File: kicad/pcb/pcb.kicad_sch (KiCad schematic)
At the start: 0 parts

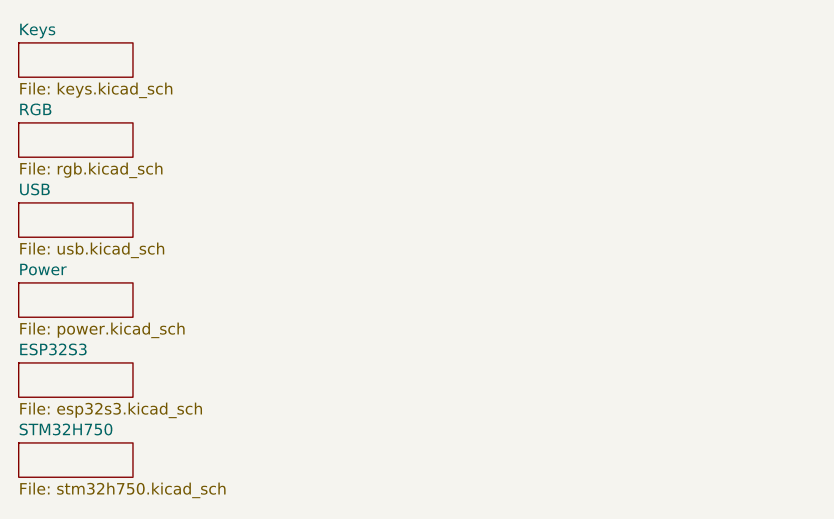
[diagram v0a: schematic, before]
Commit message: USB (almost) done + some STM progress
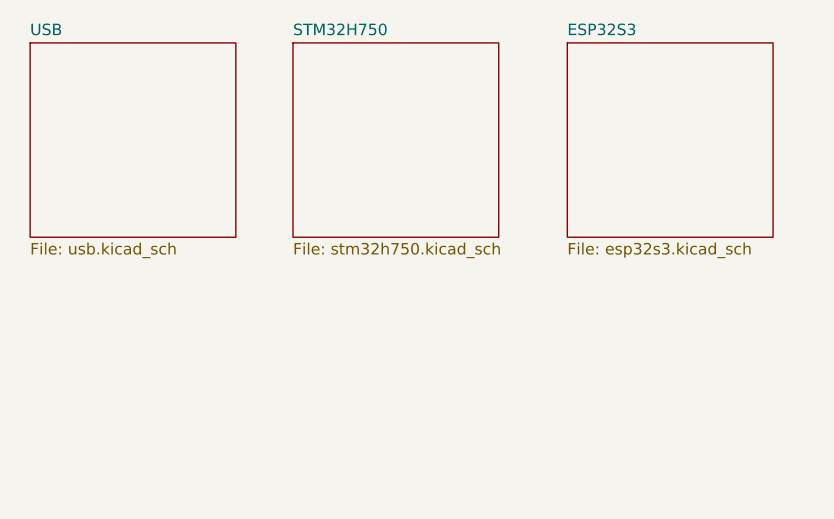
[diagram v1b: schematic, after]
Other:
- removed sheet Keys
- removed sheet Power
- removed sheet RGB
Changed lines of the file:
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@@
 (kicad_sch (version 20230121) (generator eeschema)
   (paper "A5")
-  (sheet (at 13.97 59.69) (size 12.7 3.81) (fields_autoplaced)
+  (sheet (at 44.45 15.24) (size 22.86 21.59) (fields_autoplaced)
     (stroke (width 0.1524) (type solid))
     (fill (color 0 0 0 0.0000))
-    (property "Sheetname" "STM32H750" (at 13.97 58.9784 0)
+    (property "Sheetname" "STM32H750" (at 44.45 14.5284 0)
       (effects (font (size 1.27 1.27)) (justify left bottom))
     )
-    (property "Sheetfile" "stm32h750.kicad_sch" (at 13.97 64.0846 0)
+    (property "Sheetfile" "stm32h750.kicad_sch" (at 44.45 37.4146 0)
       (effects (font (size 1.27 1.27)) (justify left top))
     )
     (instances
       (project "pcb"
-        (path "/3c00b562-f31c-4144-9978-9a1bbba7ab3a" (page "8"))
+        (path "/3c00b562-f31c-4144-9978-9a1bbba7ab3a" (page "2"))
       )
     )
   )
-  (sheet (at 13.97 24.13) (size 12.7 3.81) (fields_autoplaced)
+  (sheet (at 74.93 15.24) (size 22.86 21.59) (fields_autoplaced)
     (stroke (width 0.1524) (type solid))
     (fill (color 0 0 0 0.0000))
-    (property "Sheetname" "RGB" (at 13.97 23.4184 0)
+    (property "Sheetname" "ESP32S3" (at 74.93 14.5284 0)
       (effects (font (size 1.27 1.27)) (justify left bottom))
     )
-    (property "Sheetfile" "rgb.kicad_sch" (at 13.97 28.5246 0)
+    (property "Sheetfile" "esp32s3.kicad_sch" (at 74.93 37.4146 0)
       (effects (font (size 1.27 1.27)) (justify left top))
     )
@@
     )
   )
-  (sheet (at 13.97 50.8) (size 12.7 3.81) (fields_autoplaced)
+  (sheet (at 15.24 15.24) (size 22.86 21.59) (fields_autoplaced)
     (stroke (width 0.1524) (type solid))
     (fill (color 0 0 0 0.0000))
-    (property "Sheetname" "ESP32S3" (at 13.97 50.0884 0)
+    (property "Sheetname" "USB" (at 15.24 14.5284 0)
       (effects (font (size 1.27 1.27)) (justify left bottom))
     )
-    (property "Sheetfile" "esp32s3.kicad_sch" (at 13.97 55.1946 0)
+    (property "Sheetfile" "usb.kicad_sch" (at 15.24 37.4146 0)
       (effects (font (size 1.27 1.27)) (justify left top))
     )
     (instances
       (project "pcb"
-        (path "/3c00b562-f31c-4144-9978-9a1bbba7ab3a" (page "7"))
+        (path "/3c00b562-f31c-4144-9978-9a1bbba7ab3a" (page "1"))
       )
     )
-  )
-  (sheet (at 13.97 33.02) (size 12.7 3.81) (fields_autoplaced)
-    (stroke (width 0.1524) (type solid))
-    (fill (color 0 0 0 0.0000))
-    (property "Sheetname" "USB" (at 13.97 32.3084 0)
-      (effects (font (size 1.27 1.27)) (justify left bottom))
-    )
-    (property "Sheetfile" "usb.kicad_sch" (at 13.97 37.4146 0)
-      (effects (font (size 1.27 1.27)) (justify left top))
-    )
-    (instances
-      (project "pcb"
-        (path "/3c00b562-f31c-4144-9978-9a1bbba7ab3a" (page "4"))
-      )
-    )
-  )
-  (sheet (at 13.97 41.91) (size 12.7 3.81) (fields_autoplaced)
-    (stroke (width 0.1524) (type solid))
-    (fill (color 0 0 0 0.0000))
-    (property "Sheetname" "Power" (at 13.97 41.1984 0)
-      (effects (font (size 1.27 1.27)) (justify left bottom))
-    )
-    (property "Sheetfile" "power.kicad_sch" (at 13.97 46.3046 0)
-      (effects (font (size 1.27 1.27)) (justify left top))
-    )
-    (instances
-      (project "pcb"
-        (path "/3c00b562-f31c-4144-9978-9a1bbba7ab3a" (page "5"))
-      )
-    )
-  )
-  (sheet (at 13.97 15.24) (size 12.7 3.81) (fields_autoplaced)
-    (stroke (width 0.1524) (type solid))
-    (fill (color 0 0 0 0.0000))
-    (property "Sheetname" "Keys" (at 13.97 14.5284 0)
-      (effects (font (size 1.27 1.27)) (justify left bottom))
-    )
-    (property "Sheetfile" "keys.kicad_sch" (at 13.97 19.6346 0)
-      (effects (font (size 1.27 1.27)) (justify left top))
-    )
-    (instances
-      (project "pcb"
-        (path "/3c00b562-f31c-4144-9978-9a1bbba7ab3a" (page "2"))
-      )
-    )
